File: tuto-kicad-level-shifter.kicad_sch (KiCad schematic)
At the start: 0 parts

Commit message: Ajout des composants
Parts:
- added C1: 100p, symbol Device:C
- added J1, J2, J3, J4, J5, J6, J7: Conn_01x01_Pin, symbol Connector:Conn_01x01_Pin
- added R1: 200k, symbol Device:R
- added R2, R3, R4, R5: NA, symbol Device:R
- added U1: PCA9306, Package_SO:SSOP-8_2.95x2.8mm_P0.65mm, symbol Interface:PCA9306

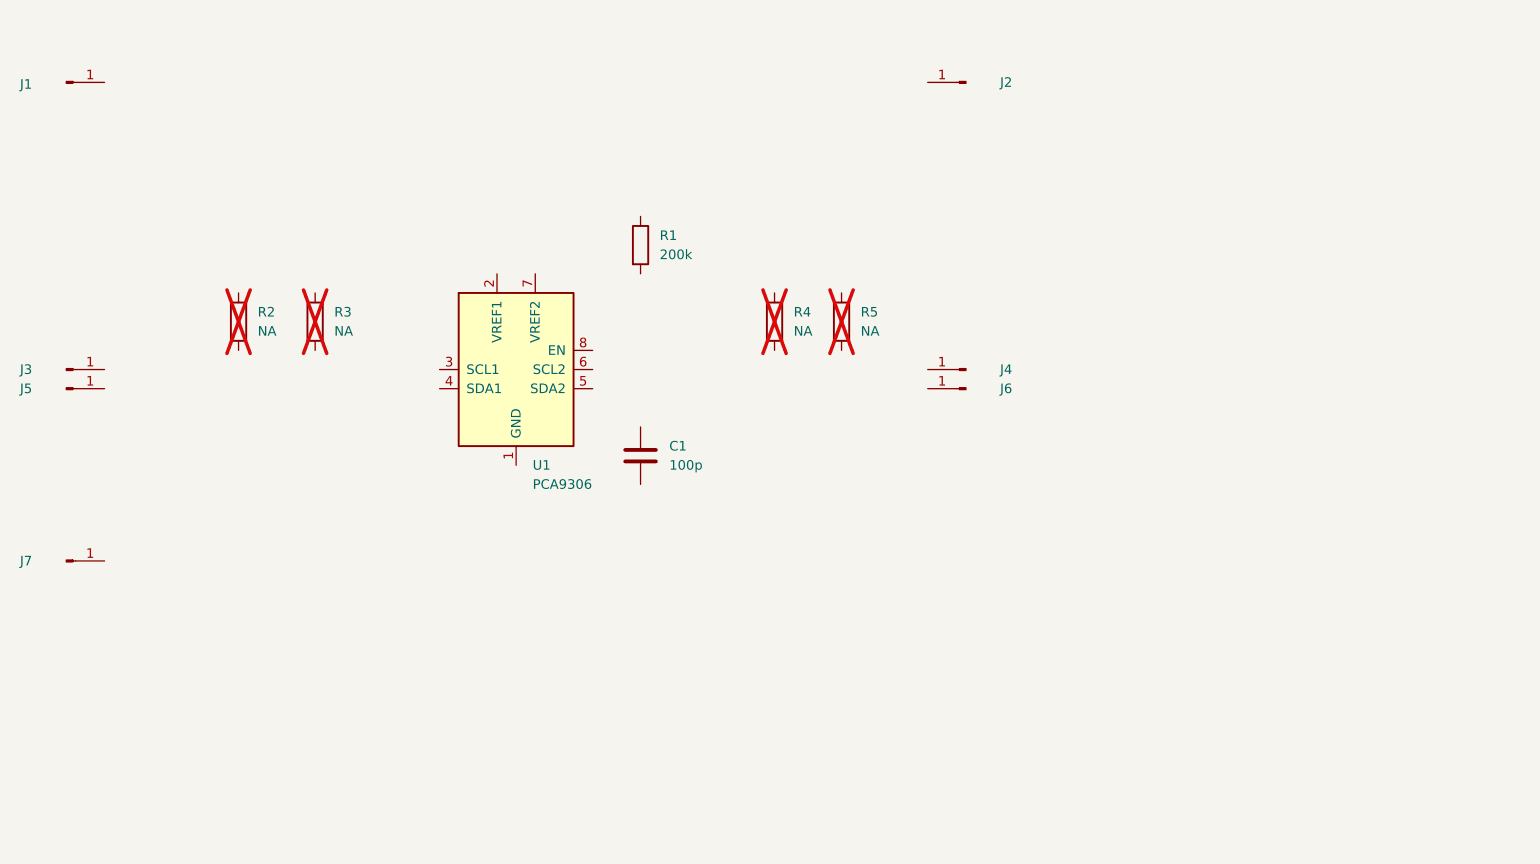
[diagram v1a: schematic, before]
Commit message: Ajouter composants d'alimentation, connexion des composants
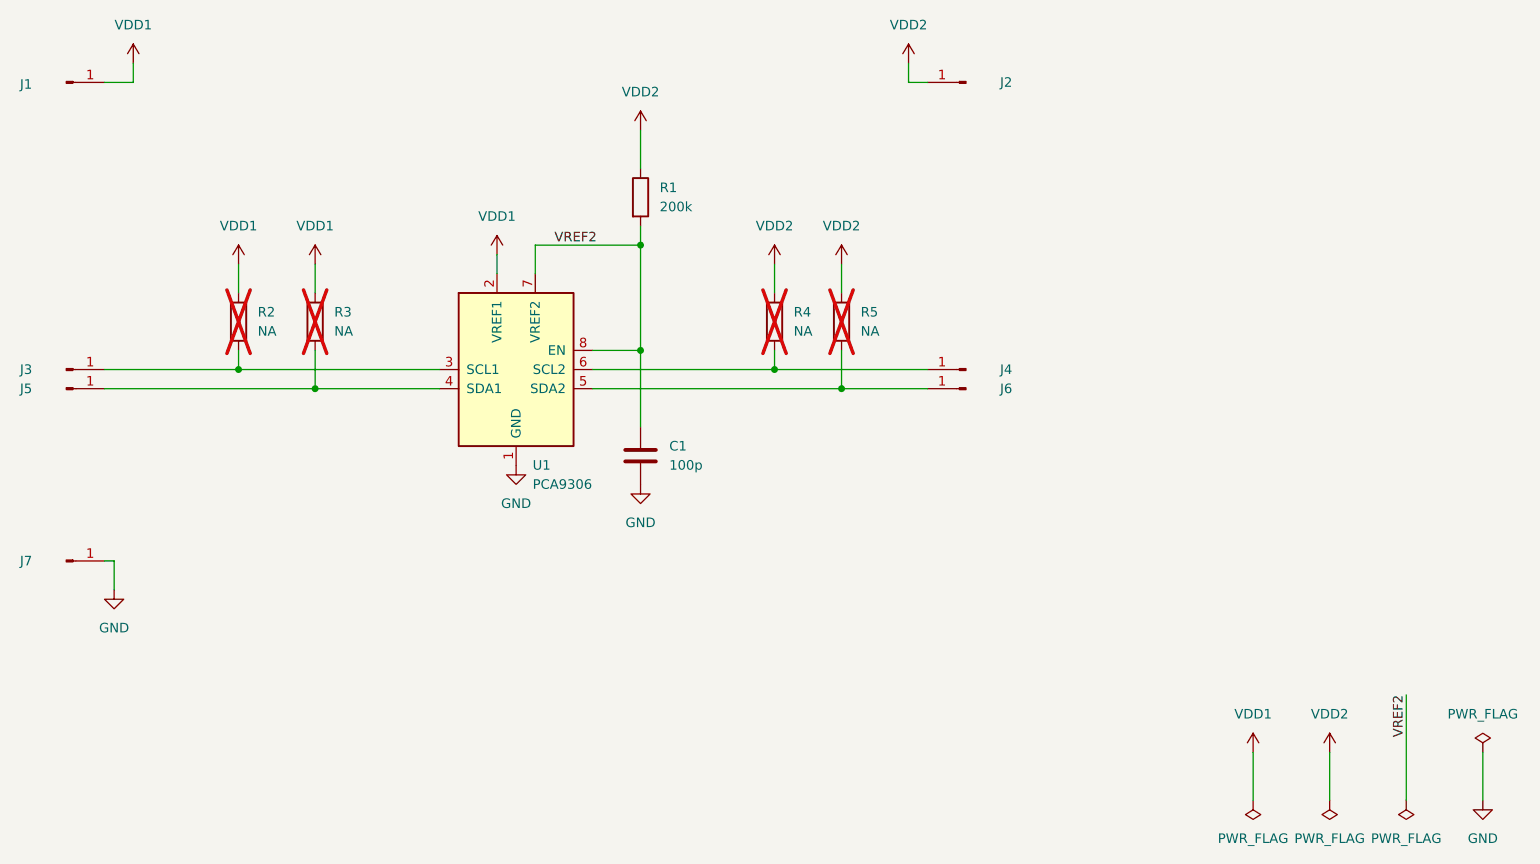
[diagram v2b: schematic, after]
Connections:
- net VDD2: now reaches R5.1
- net VDD2: now also J2.1 (Pin_1), R1.1, R4.1
- net at R5.2: now also J6.1 (Pin_1), U1.5 (SDA2)
- net VDD1: now reaches J1.1 (Pin_1)
- net VDD1: now also R2.1, R3.1, U1.2 (VREF1)
- net GND: now reaches J7.1 (Pin_1)
- net GND: now also C1.2, U1.1 (GND)
- net at R4.2: now also J4.1 (Pin_1), U1.6 (SCL2)
- net VREF2: now reaches R1.2
- net VREF2: now also C1.1, U1.7 (VREF2), U1.8 (EN)
- net at U1.3 (SCL1): now also J3.1 (Pin_1), R2.2
- net at U1.4 (SDA1): now also J5.1 (Pin_1), R3.2
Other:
- moved on the sheet: R1

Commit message: Assignation des empreintes
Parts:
- C1: footprint (none) -> Capacitor_SMD:C_0603_1608Metric
- J1, J2, J3, J4, J5, J6, J7: footprint (none) -> Connector_PinHeader_2.54mm:PinHeader_1x01_P2.54mm_Vertical
- R1, R2, R3, R4, R5: footprint (none) -> Resistor_SMD:R_0603_1608Metric
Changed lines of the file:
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@@
 			)
 		)
-		(property "Footprint" ""
+		(property "Footprint" "Resistor_SMD:R_0603_1608Metric"
 			(at 178.562 88.9 90)
 			(effects
@@
 			)
 		)
-		(property "Footprint" ""
+		(property "Footprint" "Connector_PinHeader_2.54mm:PinHeader_1x01_P2.54mm_Vertical"
 			(at 77.47 57.15 0)
 			(effects
@@
 			)
 		)
-		(property "Footprint" ""
+		(property "Footprint" "Connector_PinHeader_2.54mm:PinHeader_1x01_P2.54mm_Vertical"
 			(at 77.47 120.65 0)
 			(effects
@@
 			)
 		)
-		(property "Footprint" ""
+		(property "Footprint" "Resistor_SMD:R_0603_1608Metric"
 			(at 169.672 88.9 90)
 			(effects
@@
 			)
 		)
-		(property "Footprint" ""
+		(property "Footprint" "Resistor_SMD:R_0603_1608Metric"
 			(at 151.892 72.39 90)
 			(effects
@@
 			)
 		)
-		(property "Footprint" ""
+		(property "Footprint" "Connector_PinHeader_2.54mm:PinHeader_1x01_P2.54mm_Vertical"
 			(at 196.85 57.15 0)
 			(effects
@@
 			)
 		)
-		(property "Footprint" ""
+		(property "Footprint" "Connector_PinHeader_2.54mm:PinHeader_1x01_P2.54mm_Vertical"
 			(at 196.85 97.79 0)
 			(effects
@@
 			)
 		)
-		(property "Footprint" ""
+		(property "Footprint" "Capacitor_SMD:C_0603_1608Metric"
 			(at 154.6352 110.49 0)
 			(effects
@@
 			)
 		)
-		(property "Footprint" ""
+		(property "Footprint" "Connector_PinHeader_2.54mm:PinHeader_1x01_P2.54mm_Vertical"
 			(at 77.47 95.25 0)
 			(effects
@@
 			)
 		)
-		(property "Footprint" ""
+		(property "Footprint" "Connector_PinHeader_2.54mm:PinHeader_1x01_P2.54mm_Vertical"
 			(at 196.85 95.25 0)
 			(effects
@@
 			)
 		)
-		(property "Footprint" ""
+		(property "Footprint" "Connector_PinHeader_2.54mm:PinHeader_1x01_P2.54mm_Vertical"
 			(at 77.47 97.79 0)
 			(effects
@@
 			)
 		)
-		(property "Footprint" ""
+		(property "Footprint" "Resistor_SMD:R_0603_1608Metric"
 			(at 108.712 88.9 90)
 			(effects
@@
 			)
 		)
-		(property "Footprint" ""
+		(property "Footprint" "Resistor_SMD:R_0603_1608Metric"
 			(at 98.552 88.9 90)
 			(effects
